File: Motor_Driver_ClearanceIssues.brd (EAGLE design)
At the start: 127 x 76.2 mm, 88 parts

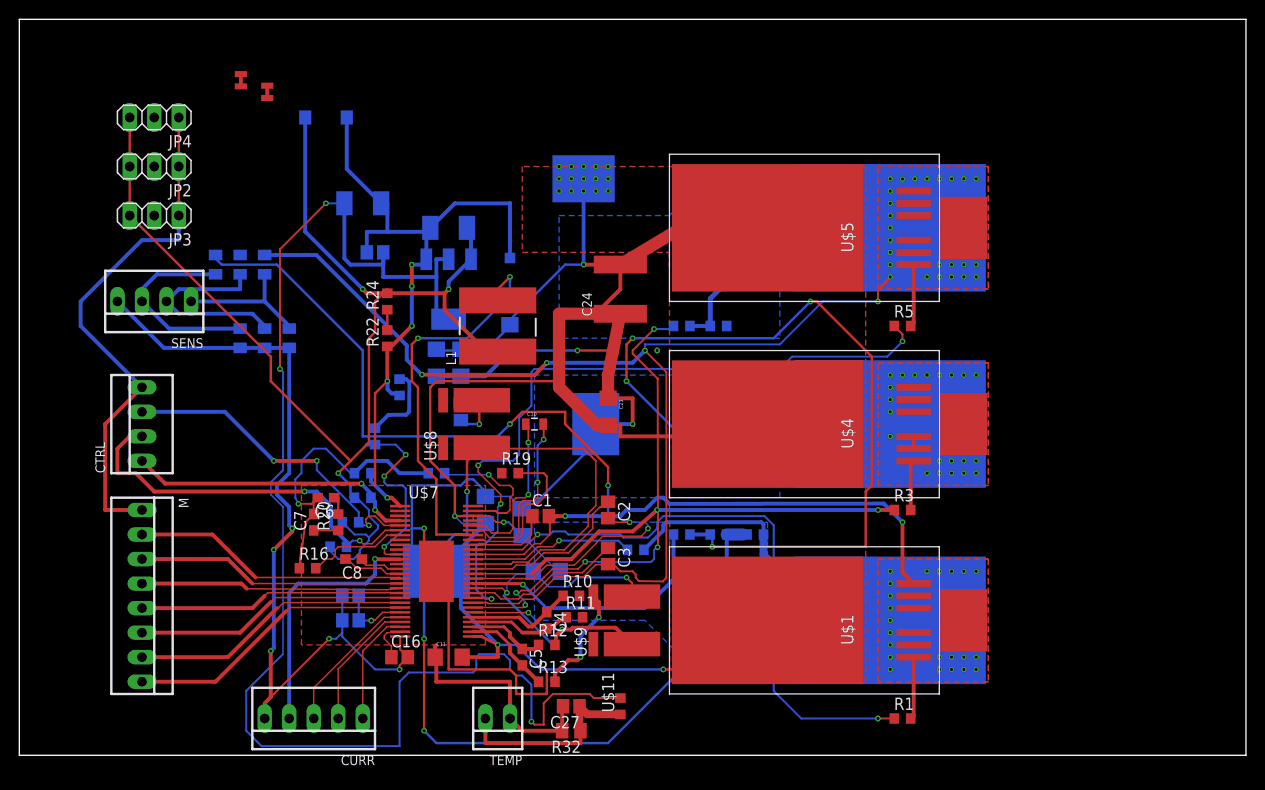
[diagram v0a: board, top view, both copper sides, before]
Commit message: removed some overlap errors and routed motor board
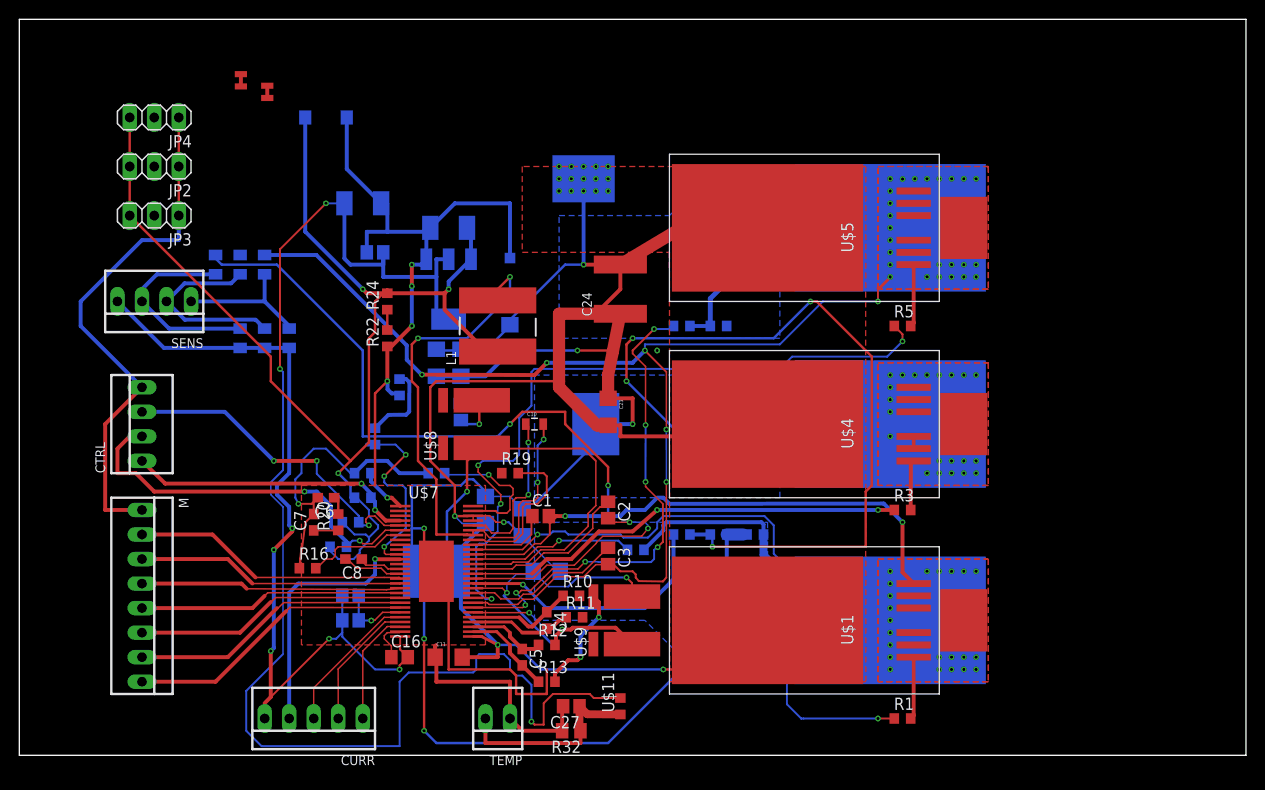
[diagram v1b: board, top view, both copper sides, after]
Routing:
- net SENS2: track 21.2 -> 20.4 mm
- net H1_LOW: track 111.2 -> 110.5 mm
- net GL_C: track 51.1 -> 51.5 mm, vias 5 -> 7
- net H3_VS: track 123.5 -> 123.6 mm, vias 19 -> 21
